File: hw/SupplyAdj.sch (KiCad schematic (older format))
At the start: 17 parts

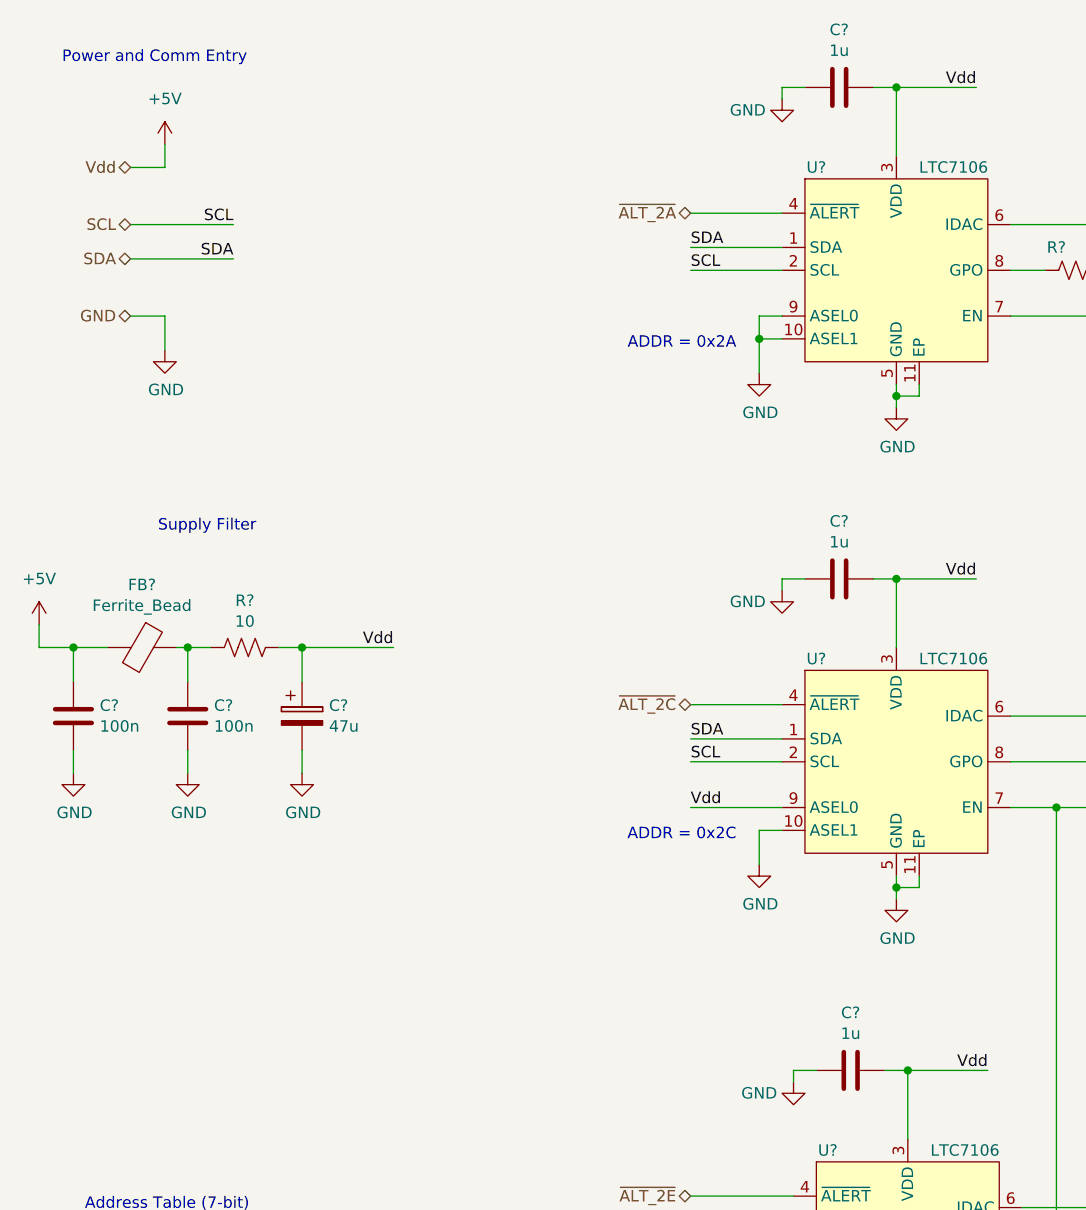
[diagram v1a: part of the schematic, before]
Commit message: Cap selections
Lots of capacitor selections & datasheet downloads

Updated LTPowerCAD model with initial compensation values for primary switcher
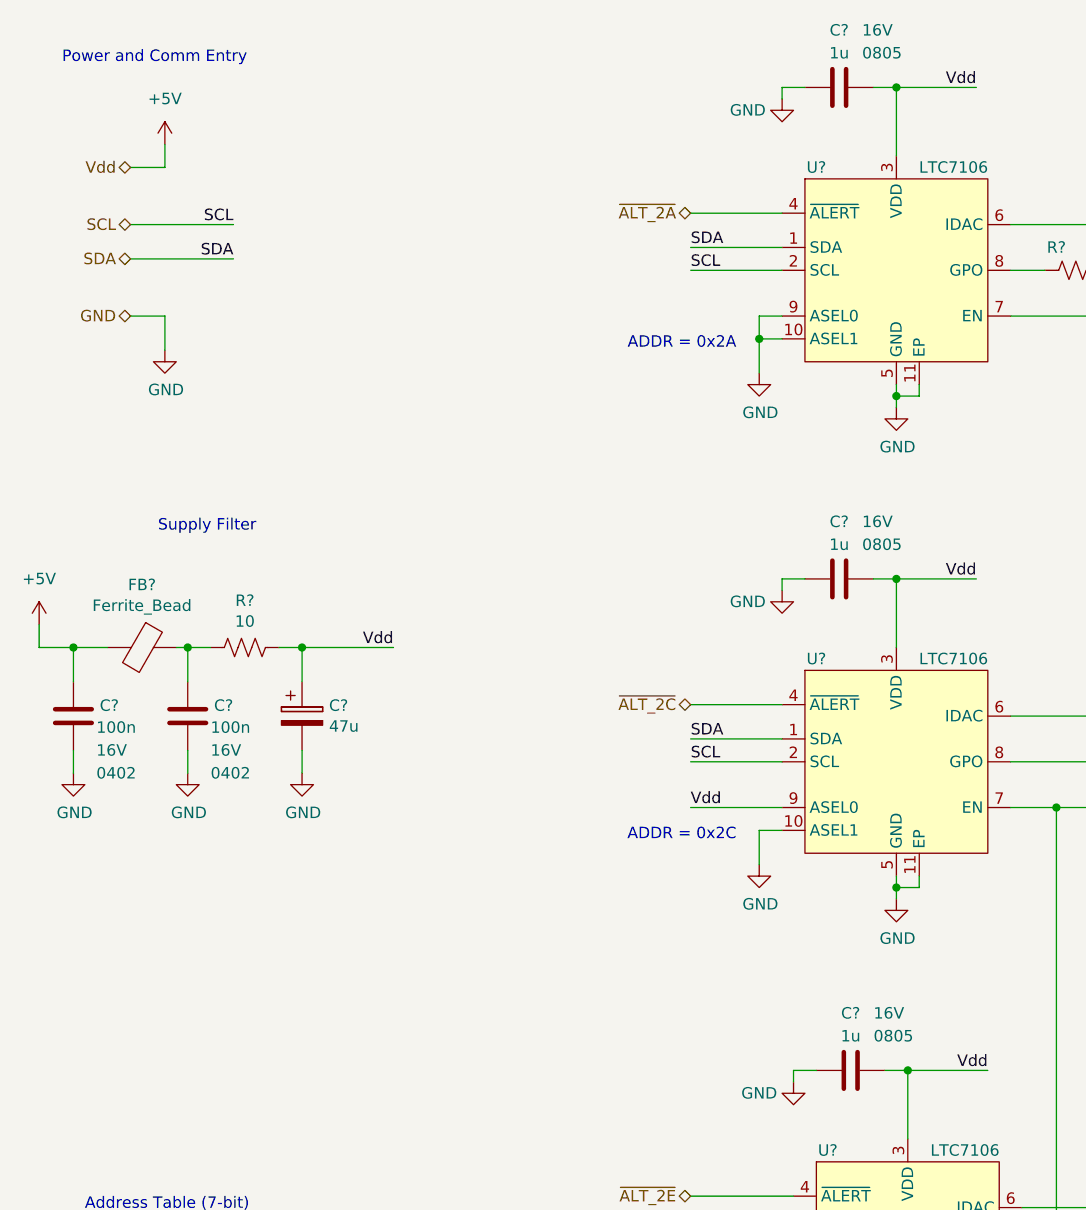
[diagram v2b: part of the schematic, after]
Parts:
- removed C? (x3): 1u, Resistor_SMD:R_0603_1608Metric, symbol Device:C
- removed C?: 100n, Resistor_SMD:R_0402_1005Metric, symbol Device:C
- added C? (x3): 1u, Resistor_SMD:R_0805_2012Metric_Pad1.15x1.40mm_HandSolder, symbol Device:C
- added C?: 100n, Resistor_SMD:R_0603_1608Metric, symbol Device:C
- C?: footprint Resistor_SMD:R_0402_1005Metric -> Resistor_SMD:R_0603_1608Metric; MfrNum (none) -> TDK_CGA2B2X5R1C104K050BA; Size (none) -> 0402; VRating (none) -> 16V
- R?: footprint Resistor_SMD:R_0603_1608Metric -> Resistor_SMD:R_0805_2012Metric
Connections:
- net +5V: now also C?.2, C?.2, C?.2
- net GND: now also C?.1, C?.1, C?.1, C?.1
- net at FB?.1, R?.2: now also C?.2
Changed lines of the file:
@@
 F 0 "R?" V 1795 3350 50  0000 C CNN
 F 1 "10" V 1886 3350 50  0000 C CNN
-F 2 "Resistor_SMD:R_0603_1608Metric" V 2040 3340 50  0001 C CNN
+F 2 "Resistor_SMD:R_0805_2012Metric" V 2040 3340 50  0001 C CNN
 F 3 "~" H 2000 3350 50  0001 C CNN
 	1    2000 3350
@@
 Text Notes 2050 2850 2    50   ~ 0
 Supply Filter
-$Comp
-L Device:C C?
-U 1 1 5E96A6EB
-P 4600 900
-F 0 "C?" V 4852 900 50  0000 C CNN
-F 1 "1u" V 4761 900 50  0000 C CNN
-F 2 "Resistor_SMD:R_0603_1608Metric" H 4638 750 50  0001 C CNN
-F 3 "" H 4600 900 50  0001 C CNN
-F 4 "TDK C1005X6S1C105K050BC" V 4600 900 50  0001 C CNN "MfrNum"
-	1    4600 900
-	0    -1   -1   0
-$EndComp
 $Comp
 L power:GND #PWR?
@@
 Wire Wire Line
 	4900 5200 5250 5200
-$Comp
-L Device:C C?
-U 1 1 5E970037
-P 4600 3050
-F 0 "C?" V 4852 3050 50  0000 C CNN
-F 1 "1u" V 4761 3050 50  0000 C CNN
-F 2 "Resistor_SMD:R_0603_1608Metric" H 4638 2900 50  0001 C CNN
-F 3 "" H 4600 3050 50  0001 C CNN
-F 4 "TDK C1005X6S1C105K050BC" V 4600 3050 50  0001 C CNN "MfrNum"
-	1    4600 3050
-	0    -1   -1   0
-$EndComp
-$Comp
-L Device:C C?
-U 1 1 5E970081
-P 4650 5200
-F 0 "C?" V 4902 5200 50  0000 C CNN
-F 1 "1u" V 4811 5200 50  0000 C CNN
-F 2 "Resistor_SMD:R_0603_1608Metric" H 4688 5050 50  0001 C CNN
-F 3 "" H 4650 5200 50  0001 C CNN
-F 4 "TDK C1005X6S1C105K050BC" V 4650 5200 50  0001 C CNN "MfrNum"
-	1    4650 5200
-	0    -1   -1   0
-$EndComp
 $Comp
 L Device:R_US R?
@@
 ADDR = 0x2E
 $Comp
-L Device:C C?
-U 1 1 5E97AE0B
-P 1750 3650
-F 0 "C?" H 1635 3604 50  0000 R CNN
-F 1 "100n" H 1635 3695 50  0000 R CNN
-F 2 "Resistor_SMD:R_0402_1005Metric" H 1788 3500 50  0001 C CNN
-F 3 "" H 1750 3650 50  0001 C CNN
-	1    1750 3650
-	-1   0    0    1
-$EndComp
-$Comp
 L power:GND #PWR?
 U 1 1 5E97AE56
@@
 P 1250 3650
 F 0 "C?" H 1135 3604 50  0000 R CNN
-F 1 "100n" H 1135 3695 50  0000 R CNN
-F 2 "Resistor_SMD:R_0402_1005Metric" H 1288 3500 50  0001 C CNN
+F 1 "100n" H 1150 3700 50  0000 R CNN
+F 2 "Resistor_SMD:R_0603_1608Metric" H 1288 3500 50  0001 C CNN
 F 3 "" H 1250 3650 50  0001 C CNN
+F 4 "TDK_CGA2B2X5R1C104K050BA" H 1250 3650 50  0001 C CNN "MfrNum"
+F 5 "16V" H 1150 3800 50  0000 R CNN "VRating"
+F 6 "0402" H 1150 3900 50  0000 R CNN "Size"
 	1    1250 3650
 	-1   0    0    1
@@
 Wire Wire Line
 	9950 3600 9950 3500
+$Comp
+L Device:C C?
+U 1 1 5EB76770
+P 4600 3050
+F 0 "C?" V 4850 3050 50  0000 C CNN
+F 1 "1u" V 4750 3050 50  0000 C CNN
+F 2 "Resistor_SMD:R_0805_2012Metric_Pad1.15x1.40mm_HandSolder" H 4638 2900 50  0001 C CNN
+F 3 "" H 4600 3050 50  0001 C CNN
+F 4 "TDK_CGA4J2X5R1C105K125AA" V 4600 3050 50  0001 C CNN "MfrNum"
+F 5 "16V" V 4850 2950 50  0000 R CNN "VRating"
+F 6 "0805" V 4750 2950 50  0000 R CNN "Size"
+	1    4600 3050
+	0    -1   -1   0
+$EndComp
+$Comp
+L Device:C C?
+U 1 1 5EB76EA5
+P 1750 3650
+F 0 "C?" H 1635 3604 50  0000 R CNN
+F 1 "100n" H 1650 3700 50  0000 R CNN
+F 2 "Resistor_SMD:R_0603_1608Metric" H 1788 3500 50  0001 C CNN
+F 3 "" H 1750 3650 50  0001 C CNN
+F 4 "TDK_CGA2B2X5R1C104K050BA" H 1750 3650 50  0001 C CNN "MfrNum"
+F 5 "16V" H 1650 3800 50  0000 R CNN "VRating"
+F 6 "0402" H 1650 3900 50  0000 R CNN "Size"
+	1    1750 3650
+	-1   0    0    1
+$EndComp
+$Comp
+L Device:C C?
+U 1 1 5EB77154
+P 4600 900
+F 0 "C?" V 4850 900 50  0000 C CNN
+F 1 "1u" V 4750 900 50  0000 C CNN
+F 2 "Resistor_SMD:R_0805_2012Metric_Pad1.15x1.40mm_HandSolder" H 4638 750 50  0001 C CNN
+F 3 "" H 4600 900 50  0001 C CNN
+F 4 "TDK_CGA4J2X5R1C105K125AA" V 4600 900 50  0001 C CNN "MfrNum"
+F 5 "16V" V 4850 800 50  0000 R CNN "VRating"
+F 6 "0805" V 4750 800 50  0000 R CNN "Size"
+	1    4600 900
+	0    -1   -1   0
+$EndComp
+$Comp
+L Device:C C?
+U 1 1 5EB771A2
+P 4650 5200
+F 0 "C?" V 4900 5200 50  0000 C CNN
+F 1 "1u" V 4800 5200 50  0000 C CNN
+F 2 "Resistor_SMD:R_0805_2012Metric_Pad1.15x1.40mm_HandSolder" H 4688 5050 50  0001 C CNN
+F 3 "" H 4650 5200 50  0001 C CNN
+F 4 "TDK_CGA4J2X5R1C105K125AA" V 4650 5200 50  0001 C CNN "MfrNum"
+F 5 "16V" V 4900 5100 50  0000 R CNN "VRating"
+F 6 "0805" V 4800 5100 50  0000 R CNN "Size"
+	1    4650 5200
+	0    -1   -1   0
+$EndComp
 $EndSCHEMATC

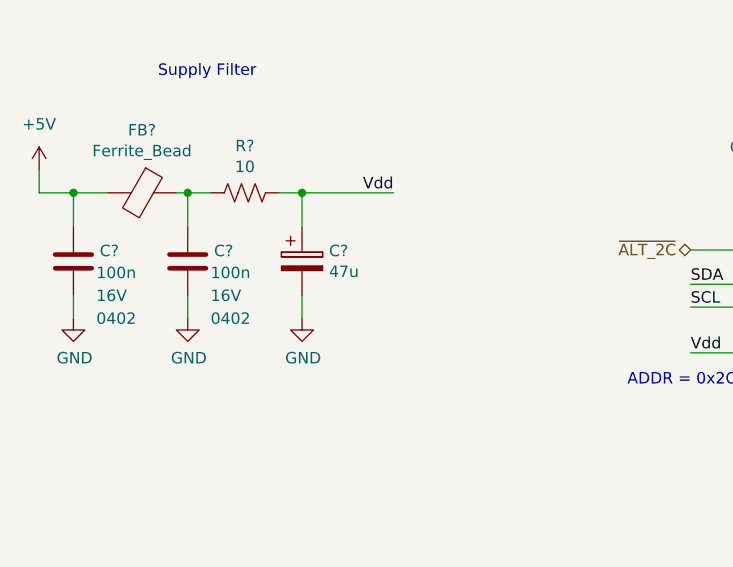
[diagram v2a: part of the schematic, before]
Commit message: more component selection
more caps selected; updated primary switcher sim file
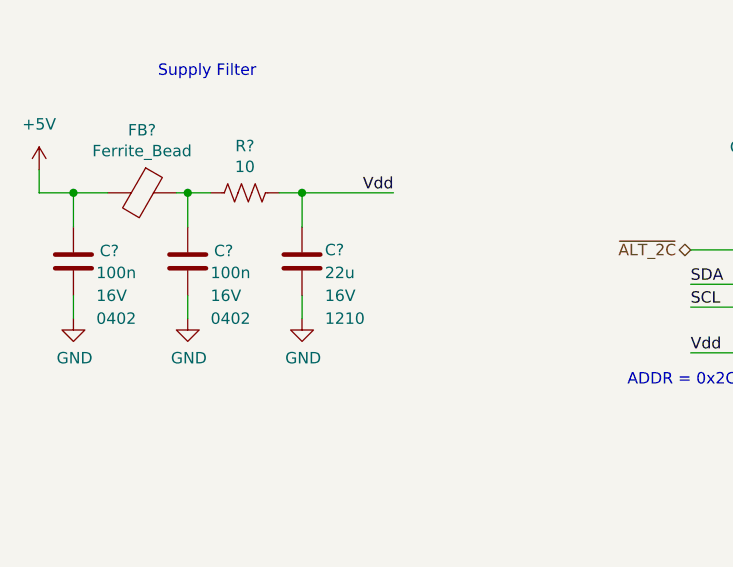
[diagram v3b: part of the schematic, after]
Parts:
- removed C?: 47u, symbol Device:CP
- added C?: 22u, symbol Device:C
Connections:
- net +5V: now also C?.1
- net GND: now also C?.2
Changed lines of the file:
@@
-$EndComp
-$Comp
-L Device:CP C?
-U 1 1 5E96694B
-P 2250 3650
-F 0 "C?" H 2368 3696 50  0000 L CNN
-F 1 "47u" H 2368 3605 50  0000 L CNN
-F 2 "" H 2288 3500 50  0001 C CNN
-F 3 "~" H 2250 3650 50  0001 C CNN
-F 4 "Wurth 875105242006" H 2250 3650 50  0001 C CNN "MfrNum"
-	1    2250 3650
-	1    0    0    -1
 $EndComp
 $Comp
@@
 	0    -1   -1   0
 $EndComp
+$Comp
+L Device:C C?
+U 1 1 5EB92034
+P 2250 3650
+AR Path="/5E84FADE/5EB92034" Ref="C?"  Part="1"
+AR Path="/5E918E7D/5EB92034" Ref="C?"  Part="1"
+F 0 "C?" H 2350 3700 50  0000 L CNN
+F 1 "22u" H 2350 3600 50  0000 L CNN
+F 2 "" H 2288 3500 50  0001 C CNN
+F 3 "~" H 2250 3650 50  0001 C CNN
+F 4 "TDK_C3225X5R1C226K250AA" H 2250 3650 50  0001 C CNN "MfrNum"
+F 5 "16V" H 2350 3500 50  0000 L CNN "VRating"
+F 6 "1210" H 2350 3400 50  0000 L CNN "Size"
+	1    2250 3650
+	1    0    0    -1
+$EndComp
 $EndSCHEMATC
